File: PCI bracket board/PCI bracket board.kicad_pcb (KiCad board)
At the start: 2 copper layers, 27.7 x 101 mm, 13 parts, among them J1 combine grounds, J3 microphone (pink), J4 line out (blue), J5 speaker in (green), J6 speaker out (black), J7 serial

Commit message: generated gerbers
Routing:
- net GNDA: vias 22 -> 16
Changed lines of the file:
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@@
       (layerselection 0x00010fc_ffffffff)
       (disableapertmacros false)
-      (usegerberextensions false)
+      (usegerberextensions true)
       (usegerberattributes true)
       (usegerberadvancedattributes true)
@@
       (plotinvisibletext false)
       (sketchpadsonfab false)
-      (subtractmaskfromsilk false)
+      (subtractmaskfromsilk true)
       (outputformat 1)
       (mirror false)
-      (drillshape 1)
+      (drillshape 0)
       (scaleselection 1)
-      (outputdirectory "")
+      (outputdirectory "PCI bracket board-gerbers")
     )
   )
@@
   (segment (start 15.5844 31.5518) (end 18.1244 34.0918) (width 1) (layer "F.Cu") (net 7))
   (via (at 25.4 7.62) (size 0.8) (drill 0.4) (layers "F.Cu" "B.Cu") (free) (net 7))
-  (via (at 12.065 37.465) (size 0.8) (drill 0.4) (layers "F.Cu" "B.Cu") (free) (net 7))
   (via (at 13.335 2.54) (size 0.8) (drill 0.4) (layers "F.Cu" "B.Cu") (free) (net 7))
   (via (at 18.415 2.54) (size 0.8) (drill 0.4) (layers "F.Cu" "B.Cu") (free) (net 7))
-  (via (at 12.065 35.56) (size 0.8) (drill 0.4) (layers "F.Cu" "B.Cu") (free) (net 7))
-  (via (at 12.065 39.37) (size 0.8) (drill 0.4) (layers "F.Cu" "B.Cu") (free) (net 7))
   (via (at 25.4 20.955) (size 0.8) (drill 0.4) (layers "F.Cu" "B.Cu") (free) (net 7))
   (via (at 15.24 8.89) (size 0.8) (drill 0.4) (layers "F.Cu" "B.Cu") (free) (net 7))
   (via (at 19.05 53.975) (size 0.8) (drill 0.4) (layers "F.Cu" "B.Cu") (free) (net 7))
-  (via (at 12.065 41.275) (size 0.8) (drill 0.4) (layers "F.Cu" "B.Cu") (free) (net 7))
   (via (at 25.4 15.24) (size 0.8) (drill 0.4) (layers "F.Cu" "B.Cu") (free) (net 7))
   (via (at 25.4 50.8) (size 0.8) (drill 0.4) (layers "F.Cu" "B.Cu") (free) (net 7))
@@
   (via (at 22.225 3.175) (size 0.8) (drill 0.4) (layers "F.Cu" "B.Cu") (free) (net 7))
   (via (at 25.4 41.275) (size 0.8) (drill 0.4) (layers "F.Cu" "B.Cu") (free) (net 7))
-  (via (at 12.065 29.21) (size 0.8) (drill 0.4) (layers "F.Cu" "B.Cu") (free) (net 7))
-  (via (at 13.335 29.21) (size 0.8) (drill 0.4) (layers "F.Cu" "B.Cu") (free) (net 7))
   (via (at 25.4 26.67) (size 0.8) (drill 0.4) (layers "F.Cu" "B.Cu") (free) (net 7))
   (via (at 25.4 45.72) (size 0.8) (drill 0.4) (layers "F.Cu" "B.Cu") (free) (net 7))

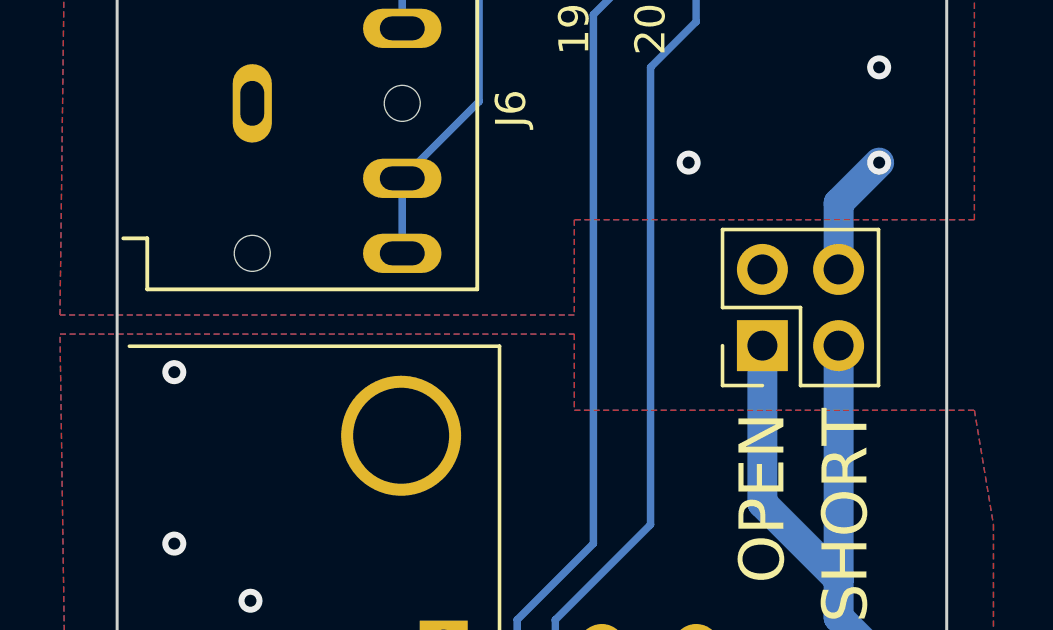
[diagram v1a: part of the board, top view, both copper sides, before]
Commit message: updated copper fill
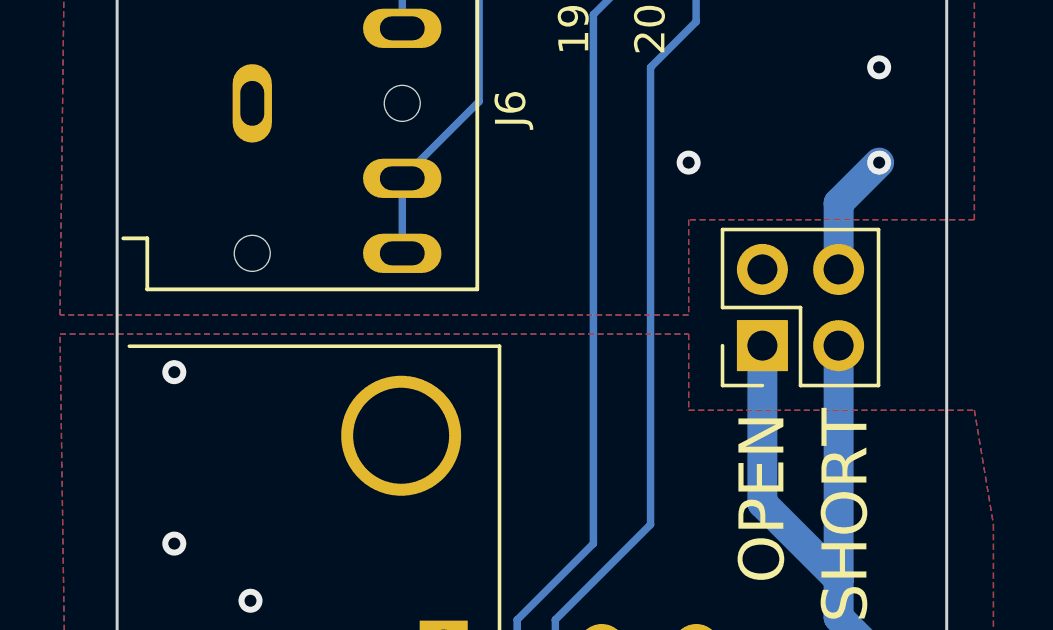
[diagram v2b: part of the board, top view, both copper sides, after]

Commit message: updated gerbers
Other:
- board text added: "Make sure the power supply ground on the plusdeck is common with the serial port ground or short the jumper"
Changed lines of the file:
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@@
     (effects (font (size 0.7 0.7) (thickness 0.1)) (justify mirror))
   )
-  (gr_text "BTO Plusdeck 2C reproduction PCI slot board" (at 22.225 81.915 90) (layer "B.SilkS")
+  (gr_text "BTO Plusdeck 2C reproduction PCI slot board" (at 23.876 35.56 90) (layer "B.SilkS")
     (effects (font (size 1 1) (thickness 0.15)) (justify mirror))
   )
@@
     (effects (font (size 0.7 0.7) (thickness 0.1)) (justify mirror))
   )
+  (gr_text "Make sure the power supply ground\non the plusdeck is common with\nthe serial port ground\nor short the jumper" (at 26.924 66.294 90) (layer "B.SilkS")
+    (effects (font (size 1 1) (thickness 0.15)) (justify left bottom mirror))
+  )
   (gr_text "Rx" (at 20.32 46.99) (layer "B.SilkS")

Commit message: updates before posting
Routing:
- net GNDA: track 7.71 -> 17.2 mm
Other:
- board text added: "5"
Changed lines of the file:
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@@
     (effects (font (size 1.5 1.5) (thickness 0.3)))
+  )
+  (gr_text "5" (at 13.97 81.28 90) (layer "F.SilkS")
+    (effects (font (size 1 1) (thickness 0.15)))
   )
   (segment (start 11.275931 78.74) (end 10.886331 78.3504) (width 0.25) (layer "F.Cu") (net 1))
@@
   (segment (start 24.0488 60.076) (end 24.0488 67.8638) (width 1) (layer "B.Cu") (net 5))
   (segment (start 15.5844 31.5518) (end 18.1244 34.0918) (width 1) (layer "F.Cu") (net 7))
+  (segment (start 15.5844 31.5518) (end 13.7718 31.5518) (width 1) (layer "F.Cu") (net 7))
+  (segment (start 14.1162 33.02) (end 13.97 32.8738) (width 1) (layer "F.Cu") (net 7))
+  (segment (start 15.5844 31.5518) (end 13.8776 29.845) (width 1) (layer "F.Cu") (net 7))
+  (segment (start 13.7718 31.5518) (end 13.335 31.115) (width 1) (layer "F.Cu") (net 7))
+  (segment (start 15.5844 31.5518) (end 14.1162 33.02) (width 1) (layer "F.Cu") (net 7))
+  (segment (start 13.97 32.8738) (end 13.97 30.48) (width 1) (layer "F.Cu") (net 7))
   (via (at 25.4 7.62) (size 0.8) (drill 0.4) (layers "F.Cu" "B.Cu") (free) (net 7))
   (via (at 13.335 2.54) (size 0.8) (drill 0.4) (layers "F.Cu" "B.Cu") (free) (net 7))
@@
     )
   )
+  (zone (net 0) (net_name "") (layers "F&B.Cu") (hatch edge 0.5)
+    (connect_pads (clearance 0))
+    (min_thickness 0.25) (filled_areas_thickness no)
+    (keepout (tracks not_allowed) (vias not_allowed) (pads not_allowed) (copperpour not_allowed) (footprints allowed))
+    (fill (thermal_gap 0.5) (thermal_bridge_width 0.5))
+    (polygon
+      (pts
+        (xy 1.27 5.715)
+        (xy -0.635 7.62)
+        (xy -0.635 5.715)
+      )
+    )
+  )
+  (zone (net 0) (net_name "") (layers "F&B.Cu") (hatch edge 0.5)
+    (connect_pads (clearance 0))
+    (min_thickness 0.25) (filled_areas_thickness no)
+    (keepout (tracks not_allowed) (vias not_allowed) (pads not_allowed) (copperpour not_allowed) (footprints allowed))
+    (fill (thermal_gap 0.5) (thermal_bridge_width 0.5))
+    (polygon
+      (pts
+        (xy 27.94 55.245)
+        (xy 26.67 56.515)
+        (xy 26.67 61.595)
+        (xy 27.94 62.865)
+      )
+    )
+  )
   (zone (net 0) (net_name "") (layers "F&B.Cu") (hatch edge 0.508)
     (connect_pads (clearance 0))
@@
         (xy 19.05 59.055)
         (xy -1.905 59.055)
-        (xy -1.27 6.985)
-        (xy 11.43 6.985)
+        (xy -1.27 6.35)
+        (xy 11.43 6.35)
         (xy 11.43 -0.635)
         (xy 28.575 -0.635)
@@
         (xy 28.575 62.23)
         (xy 29.21 66.04)
+      )
+    )
+  )
+  (zone (net 0) (net_name "") (layers "F&B.Cu") (hatch edge 0.5)
+    (connect_pads (clearance 0))
+    (min_thickness 0.25) (filled_areas_thickness no)
+    (keepout (tracks not_allowed) (vias not_allowed) (pads not_allowed) (copperpour not_allowed) (footprints allowed))
+    (fill (thermal_gap 0.5) (thermal_bridge_width 0.5))
+    (polygon
+      (pts
+        (xy 12.7 -0.635)
+        (xy 10.795 1.27)
+        (xy 10.795 -0.635)
       )
     )
@@
       )
     )
+  )
+  (zone (net 0) (net_name "") (layer "B.Cu") (hatch edge 0.5)
+    (connect_pads (clearance 0))
+    (min_thickness 0.25) (filled_areas_thickness no)
+    (keepout (tracks not_allowed) (vias not_allowed) (pads not_allowed) (copperpour not_allowed) (footprints allowed))
+    (fill (thermal_gap 0.5) (thermal_bridge_width 0.5))
+    (polygon
+      (pts
+        (xy 19.685 56.515)
+        (xy 18.415 55.245)
+        (xy 18.415 62.865)
+        (xy 19.685 61.595)
+      )
+    )
+  )
+  (zone (net 0) (net_name "") (layer "B.Cu") (hatch edge 0.5)
+    (connect_pads (clearance 0))
+    (min_thickness 0.25) (filled_areas_thickness no)
+    (keepout (tracks not_allowed) (vias not_allowed) (pads not_allowed) (copperpour not_allowed) (footprints allowed))
+    (fill (thermal_gap 0.5) (thermal_bridge_width 0.5))
+    (polygon
+      (pts
+        (xy 15.24 58.42)
+        (xy 14.605 59.055)
+        (xy 14.605 59.69)
+        (xy 15.24 60.325)
+      )
+    )
